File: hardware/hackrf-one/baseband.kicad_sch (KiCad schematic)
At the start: 136 parts, among them P14 XCVR_CLKOUT, P15 INTR, P16 CLKIN, P18 OEB, P2 CLKOUT, P36 VAA, P37 SCL, P38 SDA, P39 SSP1_SCK, P40 SSP1_MOSI, P41 SSP1_MISO, P53 CS_XCVR, P54 CS_AD, P55 TXENABLE, P56 RXENABLE, P57 XTAL2, P58 GCK1, P59 GCK2, P60 SGPIO_CLK, P61 DA0, P62 DA7, P63 DD0, P64 DD9, P65 DA4, P66 DD5, P67 RSSI, P83 GND, P84 GND, P85 GND, P86 GND, P87 GND, P88 GND, P89 GND, P9 BASEBAND, P90 GND, P91 GND, P92 GND, Q3 MOSFET_P, T3 RX_BALUN, T4 TX_BALUN, U17 MAX2837, U18 MAX5864, U19 SI5351C, X1 GSG-XTAL4PIN

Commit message: Fixed minor DRCs
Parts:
- P16, P2: footprint hackrf:GSG-SMA-73251-2120 -> gsg-modules:SMA-73251-2120
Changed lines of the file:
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@@
 			)
 		)
-		(property "Footprint" "hackrf:GSG-SMA-73251-2120"
+		(property "Footprint" "gsg-modules:SMA-73251-2120"
 			(at 76.2 224.79 0)
 			(effects
@@
 			)
 		)
-		(property "Footprint" "hackrf:GSG-SMA-73251-2120"
+		(property "Footprint" "gsg-modules:SMA-73251-2120"
 			(at 154.94 243.84 0)
 			(effects

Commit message: Made draft production files for 2025 R10+
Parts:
- P16, P2: Note (none) -> DNP
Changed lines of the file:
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@@
 			)
 		)
+		(property "Note" "DNP"
+			(at 76.2 224.79 0)
+			(effects
+				(font
+					(size 1.524 1.524)
+				)
+				(hide yes)
+			)
+		)
 		(pin "1"
 		)
@@
 			(at 154.94 243.84 0)
 			(effects
+				(font
+					(size 1.524 1.524)
+				)
+				(hide yes)
+			)
+		)
+		(property "Note" "DNP"
+			(at 154.94 243.84 0)
+			(effects

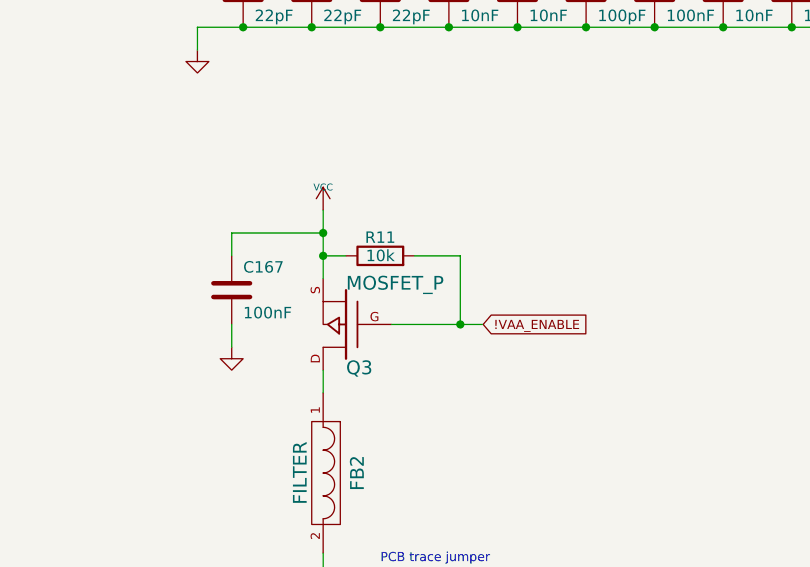
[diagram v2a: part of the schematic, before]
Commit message: Updated to move USB-C connector to save location as OpenSourceSDRLab's R10C
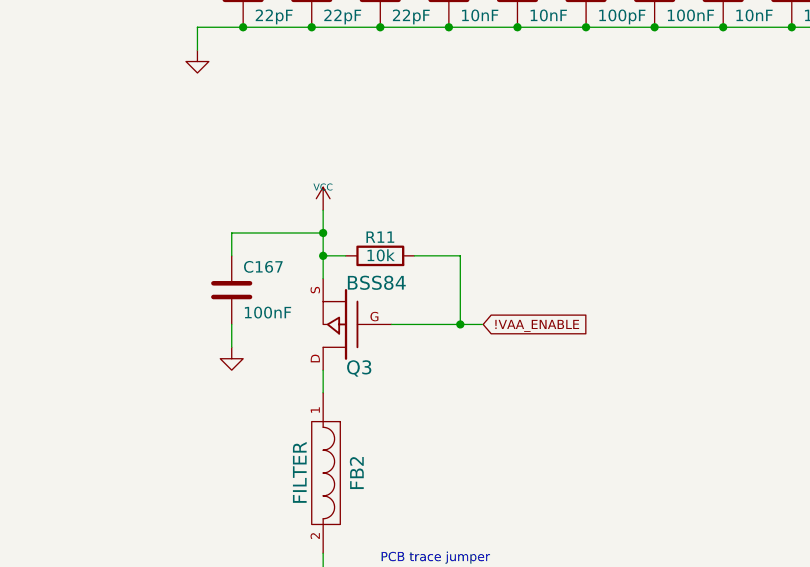
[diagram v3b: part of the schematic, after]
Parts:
- Q3: value MOSFET_P -> BSS84
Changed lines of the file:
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@@
 			)
 		)
-		(property "Value" "MOSFET_P"
+		(property "Value" "BSS84"
 			(at 53.34 64.008 0)
 			(effects

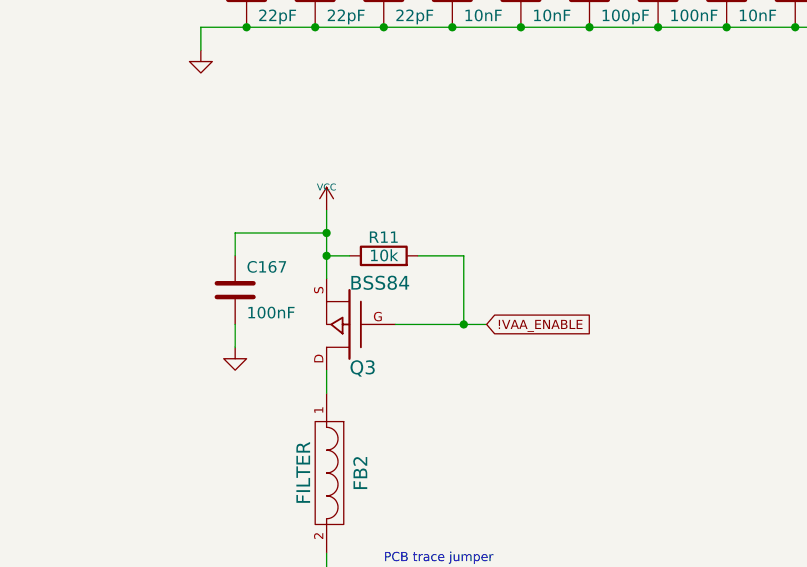
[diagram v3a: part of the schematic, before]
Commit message: Made design changes to indicate version 15. Correct Q3/4/5 part-no and LPF rotation
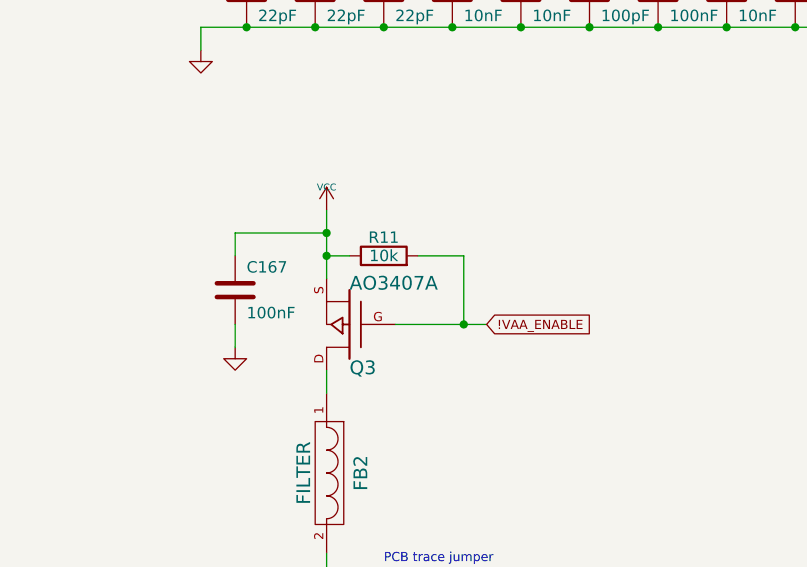
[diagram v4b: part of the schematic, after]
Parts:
- Q3: value BSS84 -> AO3407A; Manufacturer Diodes Inc. -> Alpha and Omega; Part Number DMP2305U-7 -> AO3407A
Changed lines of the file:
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@@
 			)
 		)
-		(property "Value" "BSS84"
+		(property "Value" "AO3407A"
 			(at 53.34 64.008 0)
 			(effects
@@
 			)
 		)
-		(property "Description" "MOSFET P-CH 20V 4.2A SOT-23"
+		(property "Description" "MOSFET P-CH -30V -4.3A SOT23"
 			(at 53.34 68.58 0)
 			(effects
@@
 			)
 		)
-		(property "Manufacturer" "Diodes Inc."
+		(property "Manufacturer" "Alpha and Omega"
 			(at 53.34 68.58 0)
 			(effects
@@
 			)
 		)
-		(property "Part Number" "DMP2305U-7"
+		(property "Part Number" "AO3407A"
 			(at 53.34 68.58 0)
 			(effects
